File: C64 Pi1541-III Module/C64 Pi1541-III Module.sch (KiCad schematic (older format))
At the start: 19 parts, among them J1 DC IN, J2 C64_IEC, J3 C64_IEC, J8 Module_Panel, M1 Mounting, M2 Mounting, M3 Mounting, M4 Mounting, U1 7406

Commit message: First layout done
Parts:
- added R3, R4: 10k*, resistor:R_Axial_DIN0207_L6.3mm_D2.5mm_P10.16mm_Horizontal, symbol Device:R
- R6, R7: value 330 -> 330*
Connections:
- net +3V3: now also R3.1, R4.1
- net SW2_UP: now also R3.2
- net SW3_DOWN: now also R4.2
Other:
- note added: "* R3/R4 is used with rotary encoder, not\nneeded when used with standard switches."
- note added: "* Resistor values need to be adjusted according to type\nof LED installed on front panel. Sensible values for\nbright LEDs is significantly higher than what is specified."
- moved on the sheet: J8
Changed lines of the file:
@@
 Comp ""
 Comment1 ""
-Comment2 ""
-Comment3 "build another one."
+Comment2 "anything else - consider previous versions instead."
+Comment3 "build another one. It is designed for use with 1.3\" displays and rotary encoder, for "
 Comment4 "It's a PI1541, and it's the third one I've made for almost no reason beyond wanting to"
 $EndDescr
@@
 L pi1541:Module_Panel J8
 U 1 1 62DF1416
-P 10975 7725
-F 0 "J8" H 11075 8925 50  0000 C CNN
-F 1 "Module_Panel" H 11075 8850 50  0000 C CNN
-F 2 "pi1541:Module_Panel" H 10975 7725 50  0001 C CNN
-F 3 "~" H 10975 7725 50  0001 C CNN
-	1    10975 7725
+P 10550 7800
+F 0 "J8" H 10650 9000 50  0000 C CNN
+F 1 "Module_Panel" H 10650 8925 50  0000 C CNN
+F 2 "pi1541:Module_Panel" H 10550 7800 50  0001 C CNN
+F 3 "~" H 10550 7800 50  0001 C CNN
+	1    10550 7800
 	-1   0    0    -1
 $EndComp
@@
 L power:+3.3V #PWR0118
 U 1 1 62F4338D
-P 11325 6650
-F 0 "#PWR0118" H 11325 6500 50  0001 C CNN
-F 1 "+3.3V" H 11340 6823 50  0000 C CNN
-F 2 "" H 11325 6650 50  0001 C CNN
-F 3 "" H 11325 6650 50  0001 C CNN
-	1    11325 6650
+P 10900 6675
+F 0 "#PWR0118" H 10900 6525 50  0001 C CNN
+F 1 "+3.3V" H 10915 6848 50  0000 C CNN
+F 2 "" H 10900 6675 50  0001 C CNN
+F 3 "" H 10900 6675 50  0001 C CNN
+	1    10900 6675
 	-1   0    0    -1
 $EndComp
 Wire Wire Line
-	11400 7225 11175 7225
-Wire Wire Line
-	11175 7325 11400 7325
-Wire Wire Line
-	11175 7425 11400 7425
-Wire Wire Line
-	11175 7525 11400 7525
-Wire Wire Line
-	11175 7625 11400 7625
-Text GLabel 11400 7125 2    60   Input ~ 0
+	10975 7300 10750 7300
+Wire Wire Line
+	10750 7600 10975 7600
+Wire Wire Line
+	10750 7700 10975 7700
+Text GLabel 10975 7200 2    60   Input ~ 0
 I2C_SDA
-Text GLabel 11400 7025 2    60   Input ~ 0
+Text GLabel 10975 7100 2    60   Input ~ 0
 I2C_SCL
 Wire Wire Line
-	11400 7025 11175 7025
-Wire Wire Line
-	11175 7125 11400 7125
-Wire Wire Line
-	11175 7725 11250 7725
-Wire Wire Line
-	11175 7825 11325 7825
+	10975 7100 10750 7100
+Wire Wire Line
+	10750 7200 10975 7200
+Wire Wire Line
+	10750 7800 10825 7800
+Wire Wire Line
+	10750 7900 10900 7900
 $Comp
 L power:GND #PWR07
 U 1 1 630E6531
-P 11250 7925
-F 0 "#PWR07" H 11250 7675 50  0001 C CNN
-F 1 "GND" H 11255 7752 50  0000 C CNN
-F 2 "" H 11250 7925 50  0001 C CNN
-F 3 "" H 11250 7925 50  0001 C CNN
-	1    11250 7925
+P 10825 8000
+F 0 "#PWR07" H 10825 7750 50  0001 C CNN
+F 1 "GND" H 10830 7827 50  0000 C CNN
+F 2 "" H 10825 8000 50  0001 C CNN
+F 3 "" H 10825 8000 50  0001 C CNN
+	1    10825 8000
 	-1   0    0    -1
 $EndComp
 Wire Wire Line
-	11250 7925 11250 7725
-Connection ~ 11250 7725
+	10825 8000 10825 7800
+Connection ~ 10825 7800
 $Comp
 L Device:R R6
@@
 P 5750 6650
 F 0 "R6" V 5830 6650 50  0000 C CNN
-F 1 "330" V 5750 6650 50  0000 C CNN
+F 1 "330*" V 5925 6650 50  0000 C CNN
 F 2 "resistor:R_Axial_DIN0207_L6.3mm_D2.5mm_P10.16mm_Horizontal" V 5680 6650 50  0001 C CNN
 F 3 "" H 5750 6650 50  0001 C CNN
@@
 P 5750 7625
 F 0 "R7" V 5830 7625 50  0000 C CNN
-F 1 "330" V 5750 7625 50  0000 C CNN
+F 1 "330*" V 5925 7625 50  0000 C CNN
 F 2 "resistor:R_Axial_DIN0207_L6.3mm_D2.5mm_P10.16mm_Horizontal" V 5680 7625 50  0001 C CNN
 F 3 "" H 5750 7625 50  0001 C CNN
@@
 LED_ACT
 Wire Wire Line
-	11325 6650 11325 7825
-Wire Wire Line
-	11175 6725 11250 6725
-Wire Wire Line
-	11250 6725 11250 7725
-Text GLabel 11400 7225 2    60   Input ~ 0
+	10750 6800 10825 6800
+Wire Wire Line
+	10825 6800 10825 7800
+Text GLabel 10975 7300 2    60   Input ~ 0
 SW1_ENTER
-Text GLabel 11400 7325 2    60   Input ~ 0
-SW2_UP
-Text GLabel 11400 7425 2    60   Input ~ 0
-SW3_DOWN
-Text GLabel 11400 7525 2    60   Input ~ 0
+Text GLabel 10975 7600 2    60   Input ~ 0
 SW4_BACK
-Text GLabel 11400 7625 2    60   Input ~ 0
+Text GLabel 10975 7700 2    60   Input ~ 0
 SW5_INSERT
-Text GLabel 11400 6825 2    50   Input ~ 0
+Text GLabel 10975 6900 2    50   Input ~ 0
 LED_PWR
-Text GLabel 11400 6925 2    50   Input ~ 0
+Text GLabel 10975 7000 2    50   Input ~ 0
 LED_ACT
 Wire Wire Line
-	11400 6925 11175 6925
-Wire Wire Line
-	11175 6825 11400 6825
+	10975 7000 10750 7000
+Wire Wire Line
+	10750 6900 10975 6900
 Wire Wire Line
 	3800 4300 3875 4300
@@
 Wire Notes Line
 	7100 8950 15300 8950
+Wire Wire Line
+	10750 7400 11625 7400
+$Comp
+L Device:R R3
+U 1 1 640A84BF
+P 11625 6975
+F 0 "R3" H 11695 7021 50  0000 L CNN
+F 1 "10k*" H 11695 6930 50  0000 L CNN
+F 2 "resistor:R_Axial_DIN0207_L6.3mm_D2.5mm_P10.16mm_Horizontal" V 11555 6975 50  0001 C CNN
+F 3 "~" H 11625 6975 50  0001 C CNN
+	1    11625 6975
+	1    0    0    -1
+$EndComp
+$Comp
+L Device:R R4
+U 1 1 640A9414
+P 11950 6975
+F 0 "R4" H 12020 7021 50  0000 L CNN
+F 1 "10k*" H 12020 6930 50  0000 L CNN
+F 2 "resistor:R_Axial_DIN0207_L6.3mm_D2.5mm_P10.16mm_Horizontal" V 11880 6975 50  0001 C CNN
+F 3 "~" H 11950 6975 50  0001 C CNN
+	1    11950 6975
+	1    0    0    -1
+$EndComp
+Wire Wire Line
+	11625 7125 11625 7400
+Wire Wire Line
+	11950 7125 11950 7500
+Wire Wire Line
+	11950 6750 11950 6825
+Wire Wire Line
+	10900 6675 10900 7900
+$Comp
+L power:+3.3V #PWR0110
+U 1 1 640EF8C9
+P 11625 6675
+F 0 "#PWR0110" H 11625 6525 50  0001 C CNN
+F 1 "+3.3V" H 11640 6848 50  0000 C CNN
+F 2 "" H 11625 6675 50  0001 C CNN
+F 3 "" H 11625 6675 50  0001 C CNN
+	1    11625 6675
+	-1   0    0    -1
+$EndComp
+Wire Wire Line
+	11950 7500 12050 7500
+Text GLabel 12050 7500 2    60   Input ~ 0
+SW3_DOWN
+Text GLabel 12050 7400 2    60   Input ~ 0
+SW2_UP
+Text Notes 12325 6900 0    50   ~ 0
+* R3/R4 is used with rotary encoder, not\nneeded when used with standard switches.
+Wire Wire Line
+	11625 6675 11625 6750
+Wire Wire Line
+	10750 7500 11950 7500
+Connection ~ 11950 7500
+Wire Wire Line
+	11625 7400 12050 7400
+Connection ~ 11625 7400
+Wire Wire Line
+	11625 6750 11950 6750
+Connection ~ 11625 6750
+Wire Wire Line
+	11625 6750 11625 6825
+Text Notes 4675 8375 0    50   ~ 0
+* Resistor values need to be adjusted according to type\nof LED installed on front panel. Sensible values for\nbright LEDs is significantly higher than what is specified.
 $EndSCHEMATC

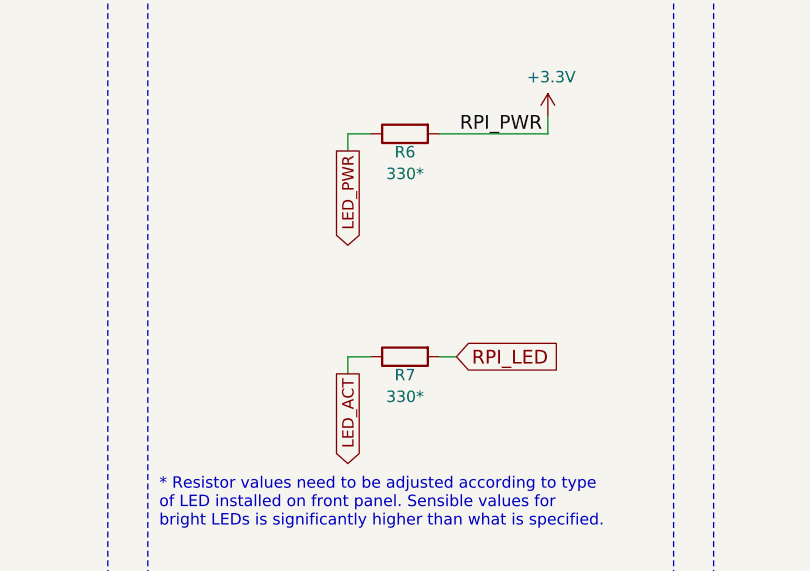
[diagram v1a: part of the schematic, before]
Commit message: Adjust LED resistor value
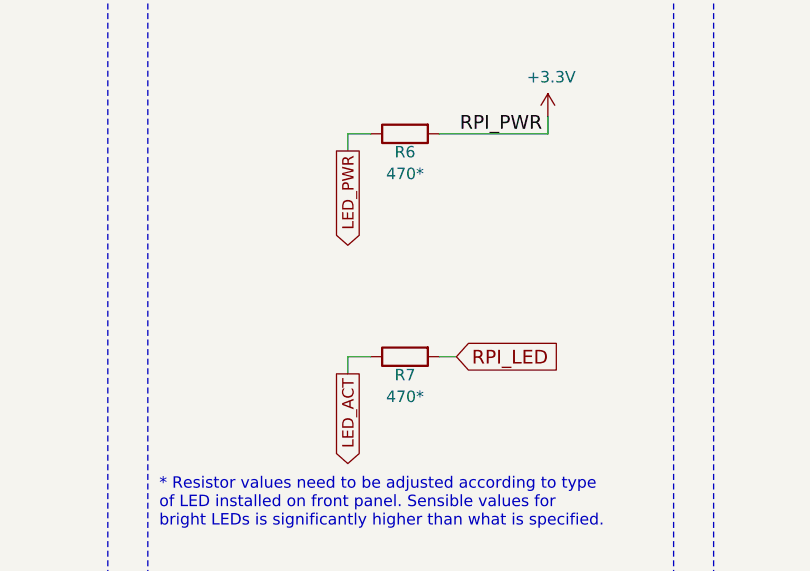
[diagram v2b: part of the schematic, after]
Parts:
- R6, R7: value 330* -> 470*
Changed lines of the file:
@@
 P 5750 6650
 F 0 "R6" V 5830 6650 50  0000 C CNN
-F 1 "330*" V 5925 6650 50  0000 C CNN
+F 1 "470*" V 5925 6650 50  0000 C CNN
 F 2 "resistor:R_Axial_DIN0207_L6.3mm_D2.5mm_P10.16mm_Horizontal" V 5680 6650 50  0001 C CNN
 F 3 "" H 5750 6650 50  0001 C CNN
@@
 P 5750 7625
 F 0 "R7" V 5830 7625 50  0000 C CNN
-F 1 "330*" V 5925 7625 50  0000 C CNN
+F 1 "470*" V 5925 7625 50  0000 C CNN
 F 2 "resistor:R_Axial_DIN0207_L6.3mm_D2.5mm_P10.16mm_Horizontal" V 5680 7625 50  0001 C CNN
 F 3 "" H 5750 7625 50  0001 C CNN

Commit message: Exported files
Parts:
- A1: value Raspberry PI -> Raspberry PI 3A/3B
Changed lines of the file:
@@
 U 1 1 640CCE33
 P 2725 3400
-F 0 "A1" H 2100 4750 50  0000 C CNN
-F 1 "Raspberry PI" H 2100 4675 50  0000 C CNN
+F 0 "A1" H 2075 4750 50  0000 C CNN
+F 1 "Raspberry PI 3A/3B" H 2075 4675 50  0000 C CNN
 F 2 "RPI:Raspberry_Pi_3B_Socketed_THT_FaceDown_MountingHoles" H 2725 3400 50  0001 C CNN
 F 3 "https://www.raspberrypi.org/documentation/hardware/raspberrypi/schematics/rpi_SCH_3bplus_1p0_reduced.pdf" H 2725 3400 50  0001 C CNN

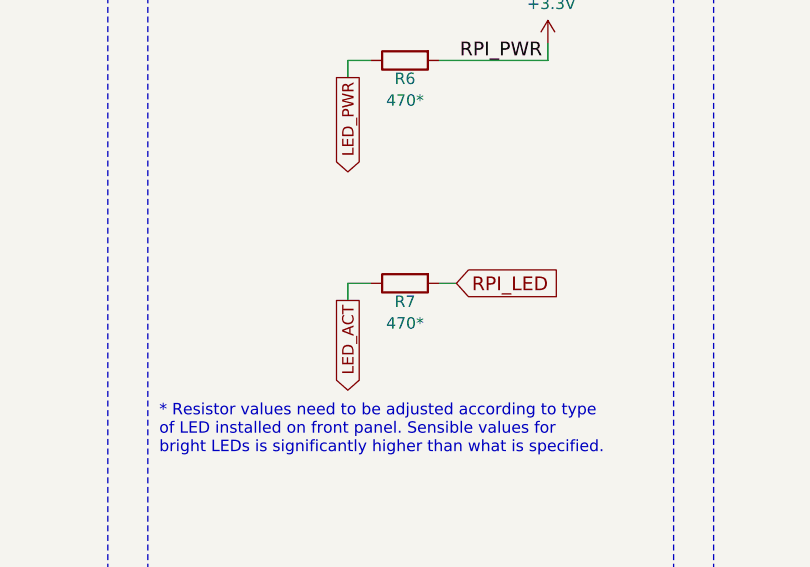
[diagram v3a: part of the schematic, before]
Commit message: Moved components around to make it easier to build
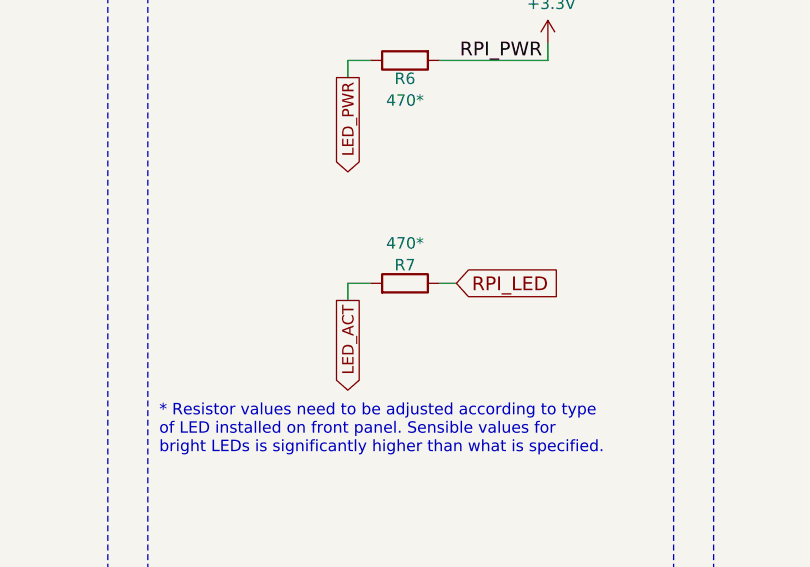
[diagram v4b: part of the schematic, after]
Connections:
- net LED_ACT: now also R7.2; no longer R7.1
- net RPI_LED: now also R7.1; no longer R7.2
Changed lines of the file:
@@
 F 3 "" H 5750 7625 50  0001 C CNN
 	1    5750 7625
-	0    -1   1    0
+	0    1    -1   0
 $EndComp
 Wire Wire Line
